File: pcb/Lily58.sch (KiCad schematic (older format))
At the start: 132 parts, among them J2 4PIN, J3 Conn_01x06_Female, J4 Conn_01x06_Female, SW1 SW_PUSH, SW10 SW_PUSH, SW11 SW_PUSH, SW12 SW_PUSH, SW13 SW_PUSH, SW14 SW_PUSH, SW15 SW_PUSH, SW16 SW_PUSH, SW17 SW_PUSH, SW18 SW_PUSH, SW19 SW_PUSH, SW2 SW_PUSH, SW20 SW_PUSH, SW21 SW_PUSH, SW22 SW_PUSH, SW23 SW_PUSH, SW24 SW_PUSH, SW25 SW_PUSH, SW26 SW_PUSH, SW27 SW_PUSH, SW28 SW_PUSH, SW29 SW_PUSH, SW3 SW_PUSH, SW4 SW_PUSH, SW5 SW_PUSH, SW6 SW_PUSH, SW7 SW_PUSH, SW8 SW_PUSH, SW9 SW_PUSH, U1 ProMicro

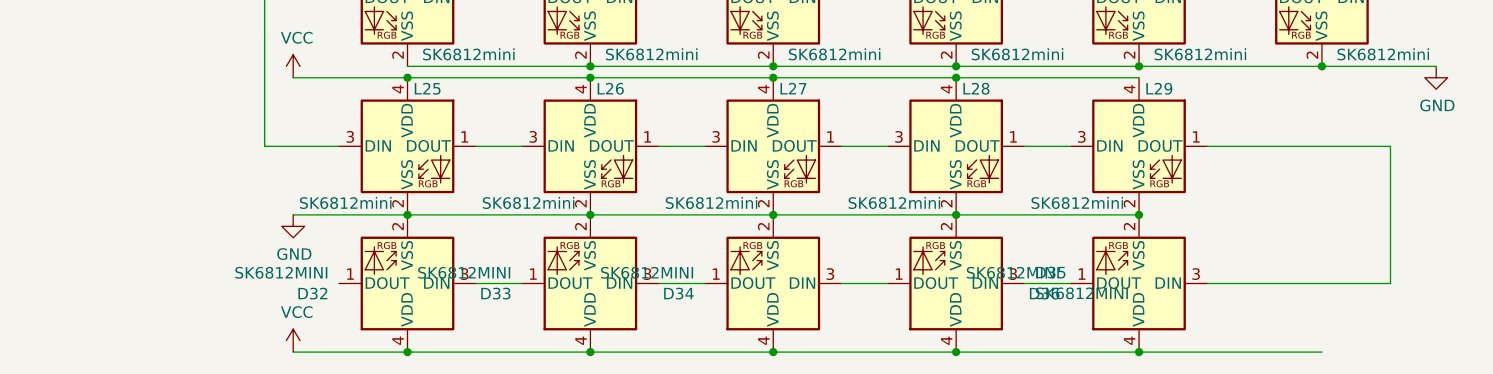
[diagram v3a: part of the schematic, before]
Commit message: refuctor pcb
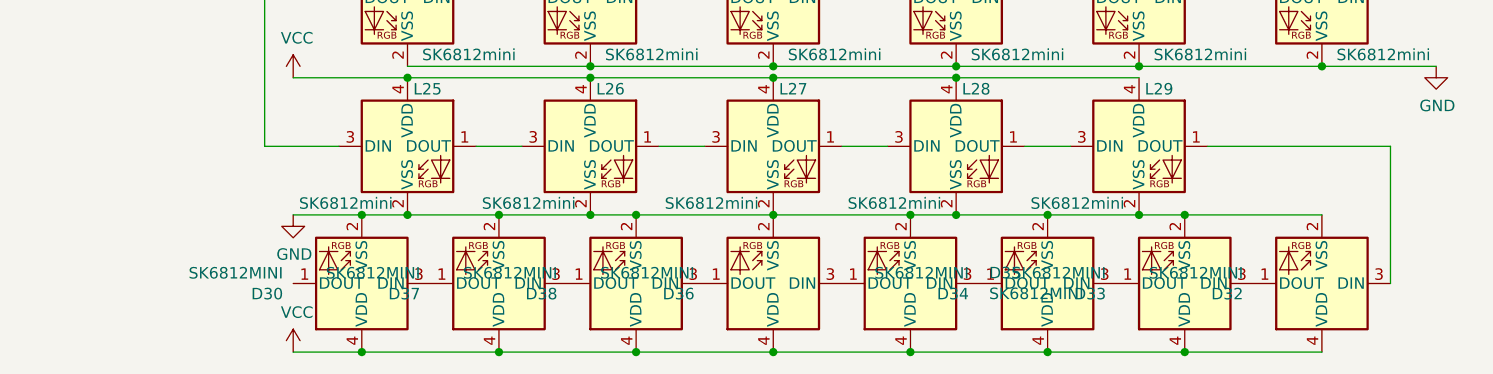
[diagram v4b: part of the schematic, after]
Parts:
- added D30, D37, D38: SK6812MINI, Lily58-footprint:SK6812MINI_underglow_rev, symbol LED:SK6812MINI
- TH3, TH4, TH5, TH6, TH7: footprint Lily58-footprint:HOLE_M2 -> Lily58-footprint:HOLE_M2_TH
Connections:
- net GND: now also D30.2 (VSS), D37.2 (VSS), D38.2 (VSS)
- net VCC: now also D30.4 (VDD), D37.4 (VDD), D38.4 (VDD)
- net at L29.1 (DOUT): now also D32.3 (DIN); no longer D36.3 (DIN)
- net at D35.1 (DOUT): now also D36.3 (DIN); no longer D34.3 (DIN)
- net at D36.1 (DOUT): now also D38.3 (DIN); no longer D35.3 (DIN)
- net at D34.1 (DOUT): now also D35.3 (DIN); no longer D33.3 (DIN)
- net at D33.1 (DOUT): now also D34.3 (DIN); no longer D32.3 (DIN)
- net at D32.1 (DOUT): now also D33.3 (DIN)
- new net: D37.3 (DIN), D38.1 (DOUT)
- new net: D30.3 (DIN), D37.1 (DOUT)
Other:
- moved on the sheet: D32, D33, D34, D35, D36
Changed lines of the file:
@@
 Wire Wire Line
 	6900 9650 7100 9650
-Wire Wire Line
-	7400 9950 8200 9950
 Connection ~ 7400 9950
 Connection ~ 6600 9950
-Wire Wire Line
-	6600 9950 7400 9950
 $Comp
 L LED:SK6812MINI L28
@@
 $EndComp
 Wire Wire Line
-	6600 9950 5800 9950
+	6600 9950 6200 9950
 Wire Wire Line
 	6100 9650 6300 9650
@@
 Wire Wire Line
 	8500 9650 8700 9650
-Wire Wire Line
-	8200 9950 9000 9950
 Connection ~ 8200 9950
 Wire Wire Line
@@
 	2850 8000 2650 8000
 Wire Wire Line
-	5300 9950 5800 9950
+	5300 9950 5600 9950
 Wire Wire Line
 	2350 7000 2800 7000
@@
 	3650 4350 3650 4450
 $Comp
-L Lily58-rescue:HOLE-Lily58-cache TH3
-U 1 1 5B74DA95
-P 8100 6150
-F 0 "TH3" H 8100 6150 60  0000 C CNN
-F 1 "HOLE" H 8100 6050 60  0000 C CNN
-F 2 "Lily58-footprint:HOLE_M2" H 8100 6150 60  0001 C CNN
-F 3 "" H 8100 6150 60  0000 C CNN
-	1    8100 6150
-	1    0    0    -1
-$EndComp
-$Comp
-L Lily58-rescue:HOLE-Lily58-cache TH7
-U 1 1 5B74D98F
-P 9500 6150
-F 0 "TH7" H 9500 6150 60  0000 C CNN
-F 1 "HOLE" H 9500 6050 60  0000 C CNN
-F 2 "Lily58-footprint:HOLE_M2" H 9500 6150 60  0001 C CNN
-F 3 "" H 9500 6150 60  0000 C CNN
-	1    9500 6150
-	1    0    0    -1
-$EndComp
-$Comp
-L Lily58-rescue:HOLE-Lily58-cache TH6
-U 1 1 5B74D88C
-P 9150 6150
-F 0 "TH6" H 9150 6150 60  0000 C CNN
-F 1 "HOLE" H 9150 6050 60  0000 C CNN
-F 2 "Lily58-footprint:HOLE_M2" H 9150 6150 60  0001 C CNN
-F 3 "" H 9150 6150 60  0000 C CNN
-	1    9150 6150
-	1    0    0    -1
-$EndComp
-$Comp
-L Lily58-rescue:HOLE-Lily58-cache TH5
-U 1 1 5B74D78B
-P 8800 6150
-F 0 "TH5" H 8800 6150 60  0000 C CNN
-F 1 "HOLE" H 8800 6050 60  0000 C CNN
-F 2 "Lily58-footprint:HOLE_M2" H 8800 6150 60  0001 C CNN
-F 3 "" H 8800 6150 60  0000 C CNN
-	1    8800 6150
-	1    0    0    -1
-$EndComp
-$Comp
-L Lily58-rescue:HOLE-Lily58-cache TH4
-U 1 1 5B74D1C0
-P 8450 6150
-F 0 "TH4" H 8450 6150 60  0000 C CNN
-F 1 "HOLE" H 8450 6050 60  0000 C CNN
-F 2 "Lily58-footprint:HOLE_M2" H 8450 6150 60  0001 C CNN
-F 3 "" H 8450 6150 60  0000 C CNN
-	1    8450 6150
-	1    0    0    -1
-$EndComp
-$Comp
 L LED:SK6812MINI D35
 U 1 1 6240B7F0
-P 8200 10250
-F 0 "D35" H 7856 10204 50  0000 R CNN
-F 1 "SK6812MINI" H 7856 10295 50  0000 R CNN
-F 2 "Lily58-footprint:SK6812MINI_underglow_rev" H 8250 9950 50  0001 L TNN
-F 3 "https://cdn-shop.adafruit.com/product-files/2686/SK6812MINI_REV.01-1-2.pdf" H 8300 9875 50  0001 L TNN
-	1    8200 10250
+P 8000 10250
+F 0 "D35" H 7656 10204 50  0000 R CNN
+F 1 "SK6812MINI" H 7656 10295 50  0000 R CNN
+F 2 "Lily58-footprint:SK6812MINI_underglow_rev" H 8050 9950 50  0001 L TNN
+F 3 "https://cdn-shop.adafruit.com/product-files/2686/SK6812MINI_REV.01-1-2.pdf" H 8100 9875 50  0001 L TNN
+	1    8000 10250
 	-1   0    0    1
 $EndComp
@@
 L LED:SK6812MINI D34
 U 1 1 62411127
+P 8600 10250
+F 0 "D34" H 8944 10296 50  0000 L CNN
+F 1 "SK6812MINI" H 8944 10205 50  0000 L CNN
+F 2 "Lily58-footprint:SK6812MINI_underglow_rev" H 8650 9950 50  0001 L TNN
+F 3 "https://cdn-shop.adafruit.com/product-files/2686/SK6812MINI_REV.01-1-2.pdf" H 8700 9875 50  0001 L TNN
+	1    8600 10250
+	-1   0    0    1
+$EndComp
+$Comp
+L LED:SK6812MINI D33
+U 1 1 62423173
+P 9200 10250
+F 0 "D33" H 9544 10296 50  0000 L CNN
+F 1 "SK6812MINI" H 9544 10205 50  0000 L CNN
+F 2 "Lily58-footprint:SK6812MINI_underglow_rev" H 9250 9950 50  0001 L TNN
+F 3 "https://cdn-shop.adafruit.com/product-files/2686/SK6812MINI_REV.01-1-2.pdf" H 9300 9875 50  0001 L TNN
+	1    9200 10250
+	-1   0    0    1
+$EndComp
+$Comp
+L LED:SK6812MINI D32
+U 1 1 6245421A
+P 9800 10250
+F 0 "D32" H 10144 10296 50  0000 L CNN
+F 1 "SK6812MINI" H 10144 10205 50  0000 L CNN
+F 2 "Lily58-footprint:SK6812MINI_underglow_rev" H 9850 9950 50  0001 L TNN
+F 3 "https://cdn-shop.adafruit.com/product-files/2686/SK6812MINI_REV.01-1-2.pdf" H 9900 9875 50  0001 L TNN
+	1    9800 10250
+	-1   0    0    1
+$EndComp
+$Comp
+L LED:SK6812MINI D36
+U 1 1 624C4CC2
 P 7400 10250
-F 0 "D34" H 7744 10296 50  0000 L CNN
+F 0 "D36" H 7744 10296 50  0000 L CNN
 F 1 "SK6812MINI" H 7744 10205 50  0000 L CNN
 F 2 "Lily58-footprint:SK6812MINI_underglow_rev" H 7450 9950 50  0001 L TNN
@@
 	-1   0    0    1
 $EndComp
-$Comp
-L LED:SK6812MINI D33
-U 1 1 62423173
-P 6600 10250
-F 0 "D33" H 6944 10296 50  0000 L CNN
-F 1 "SK6812MINI" H 6944 10205 50  0000 L CNN
-F 2 "Lily58-footprint:SK6812MINI_underglow_rev" H 6650 9950 50  0001 L TNN
-F 3 "https://cdn-shop.adafruit.com/product-files/2686/SK6812MINI_REV.01-1-2.pdf" H 6700 9875 50  0001 L TNN
-	1    6600 10250
-	-1   0    0    1
-$EndComp
-Connection ~ 9000 9950
-$Comp
-L LED:SK6812MINI D32
-U 1 1 6245421A
-P 5800 10250
-F 0 "D32" H 6144 10296 50  0000 L CNN
-F 1 "SK6812MINI" H 6144 10205 50  0000 L CNN
-F 2 "Lily58-footprint:SK6812MINI_underglow_rev" H 5850 9950 50  0001 L TNN
-F 3 "https://cdn-shop.adafruit.com/product-files/2686/SK6812MINI_REV.01-1-2.pdf" H 5900 9875 50  0001 L TNN
-	1    5800 10250
-	-1   0    0    1
-$EndComp
-Wire Wire Line
-	6100 10250 6300 10250
-Wire Wire Line
-	7100 10250 6900 10250
-Wire Wire Line
-	7700 10250 7900 10250
-$Comp
-L LED:SK6812MINI D36
-U 1 1 624C4CC2
-P 9000 10250
-F 0 "D36" H 9344 10296 50  0000 L CNN
-F 1 "SK6812MINI" H 9344 10205 50  0000 L CNN
-F 2 "Lily58-footprint:SK6812MINI_underglow_rev" H 9050 9950 50  0001 L TNN
-F 3 "https://cdn-shop.adafruit.com/product-files/2686/SK6812MINI_REV.01-1-2.pdf" H 9100 9875 50  0001 L TNN
-	1    9000 10250
-	-1   0    0    1
-$EndComp
-Wire Wire Line
-	8500 10250 8700 10250
 Wire Wire Line
 	9300 9650 10100 9650
 Wire Wire Line
 	10100 9650 10100 10250
-Wire Wire Line
-	9800 10550 9000 10550
-Connection ~ 6600 10550
-Connection ~ 7400 10550
-Wire Wire Line
-	7400 10550 6600 10550
-Connection ~ 8200 10550
-Wire Wire Line
-	8200 10550 7400 10550
-Connection ~ 9000 10550
-Wire Wire Line
-	9000 10550 8200 10550
 $Comp
 L power:VCC #PWR0115
@@
 	1    0    0    -1
 $EndComp
-Wire Wire Line
-	5300 10550 5800 10550
-Connection ~ 5800 10550
-Wire Wire Line
-	5800 10550 6600 10550
-Wire Wire Line
-	9300 10250 10100 10250
+$Comp
+L Lily58-rescue:HOLE-Lily58-cache TH4
+U 1 1 5B74D1C0
+P 8450 6150
+F 0 "TH4" H 8450 6150 60  0000 C CNN
+F 1 "HOLE" H 8450 6050 60  0000 C CNN
+F 2 "Lily58-footprint:HOLE_M2_TH" H 8450 6150 60  0001 C CNN
+F 3 "" H 8450 6150 60  0000 C CNN
+	1    8450 6150
+	1    0    0    -1
+$EndComp
+$Comp
+L Lily58-rescue:HOLE-Lily58-cache TH5
+U 1 1 5B74D78B
+P 8800 6150
+F 0 "TH5" H 8800 6150 60  0000 C CNN
+F 1 "HOLE" H 8800 6050 60  0000 C CNN
+F 2 "Lily58-footprint:HOLE_M2_TH" H 8800 6150 60  0001 C CNN
+F 3 "" H 8800 6150 60  0000 C CNN
+	1    8800 6150
+	1    0    0    -1
+$EndComp
+$Comp
+L Lily58-rescue:HOLE-Lily58-cache TH6
+U 1 1 5B74D88C
+P 9150 6150
+F 0 "TH6" H 9150 6150 60  0000 C CNN
+F 1 "HOLE" H 9150 6050 60  0000 C CNN
+F 2 "Lily58-footprint:HOLE_M2_TH" H 9150 6150 60  0001 C CNN
+F 3 "" H 9150 6150 60  0000 C CNN
+	1    9150 6150
+	1    0    0    -1
+$EndComp
+$Comp
+L Lily58-rescue:HOLE-Lily58-cache TH7
+U 1 1 5B74D98F
+P 9500 6150
+F 0 "TH7" H 9500 6150 60  0000 C CNN
+F 1 "HOLE" H 9500 6050 60  0000 C CNN
+F 2 "Lily58-footprint:HOLE_M2_TH" H 9500 6150 60  0001 C CNN
+F 3 "" H 9500 6150 60  0000 C CNN
+	1    9500 6150
+	1    0    0    -1
+$EndComp
+$Comp
+L Lily58-rescue:HOLE-Lily58-cache TH3
+U 1 1 5B74DA95
+P 8100 6150
+F 0 "TH3" H 8100 6150 60  0000 C CNN
+F 1 "HOLE" H 8100 6050 60  0000 C CNN
+F 2 "Lily58-footprint:HOLE_M2_TH" H 8100 6150 60  0001 C CNN
+F 3 "" H 8100 6150 60  0000 C CNN
+	1    8100 6150
+	1    0    0    -1
+$EndComp
+Connection ~ 7400 10550
+Connection ~ 8000 9950
+Wire Wire Line
+	8000 9950 8200 9950
+Connection ~ 8000 10550
+Connection ~ 8600 9950
+Wire Wire Line
+	8600 9950 9000 9950
+Connection ~ 8600 10550
+Wire Wire Line
+	7400 9950 8000 9950
+Wire Wire Line
+	6600 9950 6800 9950
+Wire Wire Line
+	8200 9950 8600 9950
+Wire Wire Line
+	5300 10550 5600 10550
+Wire Wire Line
+	7400 10550 8000 10550
+Wire Wire Line
+	8000 10550 8600 10550
+Wire Wire Line
+	8600 10550 9200 10550
+Connection ~ 9200 10550
+Wire Wire Line
+	9200 10550 9800 10550
+Wire Wire Line
+	9800 9950 9200 9950
+Connection ~ 9000 9950
+Connection ~ 9200 9950
+Wire Wire Line
+	9200 9950 9000 9950
+$Comp
+L LED:SK6812MINI D38
+U 1 1 61D96A0F
+P 6800 10250
+F 0 "D38" H 7144 10296 50  0000 L CNN
+F 1 "SK6812MINI" H 7144 10205 50  0000 L CNN
+F 2 "Lily58-footprint:SK6812MINI_underglow_rev" H 6850 9950 50  0001 L TNN
+F 3 "https://cdn-shop.adafruit.com/product-files/2686/SK6812MINI_REV.01-1-2.pdf" H 6900 9875 50  0001 L TNN
+	1    6800 10250
+	-1   0    0    1
+$EndComp
+Connection ~ 6800 9950
+Wire Wire Line
+	6800 9950 7400 9950
+Connection ~ 6800 10550
+Wire Wire Line
+	6800 10550 7400 10550
+$Comp
+L LED:SK6812MINI D37
+U 1 1 61D98064
+P 6200 10250
+F 0 "D37" H 6544 10296 50  0000 L CNN
+F 1 "SK6812MINI" H 6544 10205 50  0000 L CNN
+F 2 "Lily58-footprint:SK6812MINI_underglow_rev" H 6250 9950 50  0001 L TNN
+F 3 "https://cdn-shop.adafruit.com/product-files/2686/SK6812MINI_REV.01-1-2.pdf" H 6300 9875 50  0001 L TNN
+	1    6200 10250
+	-1   0    0    1
+$EndComp
+Connection ~ 6200 9950
+Wire Wire Line
+	6200 9950 5800 9950
+Connection ~ 6200 10550
+Wire Wire Line
+	6200 10550 6800 10550
+$Comp
+L LED:SK6812MINI D30
+U 1 1 61D997AB
+P 5600 10250
+F 0 "D30" H 5944 10296 50  0000 L CNN
+F 1 "SK6812MINI" H 5944 10205 50  0000 L CNN
+F 2 "Lily58-footprint:SK6812MINI_underglow_rev" H 5650 9950 50  0001 L TNN
+F 3 "https://cdn-shop.adafruit.com/product-files/2686/SK6812MINI_REV.01-1-2.pdf" H 5700 9875 50  0001 L TNN
+	1    5600 10250
+	-1   0    0    1
+$EndComp
+Connection ~ 5600 9950
+Wire Wire Line
+	5600 9950 5800 9950
+Connection ~ 5600 10550
+Wire Wire Line
+	5600 10550 6200 10550
 $EndSCHEMATC

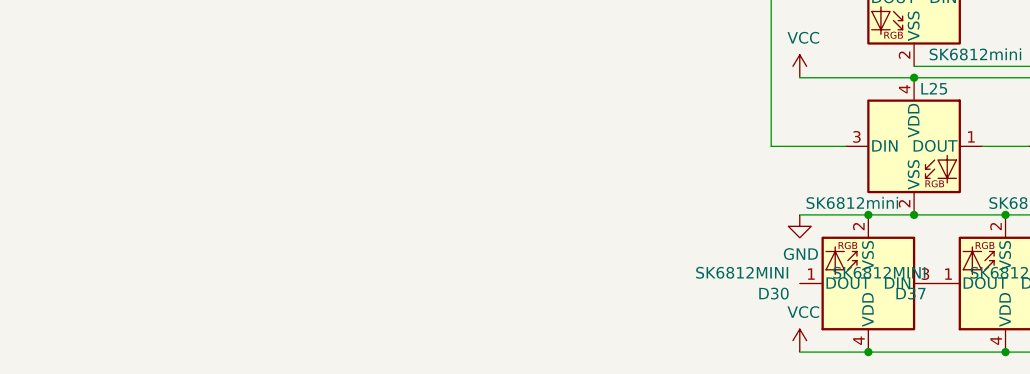
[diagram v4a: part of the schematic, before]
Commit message: add underglow
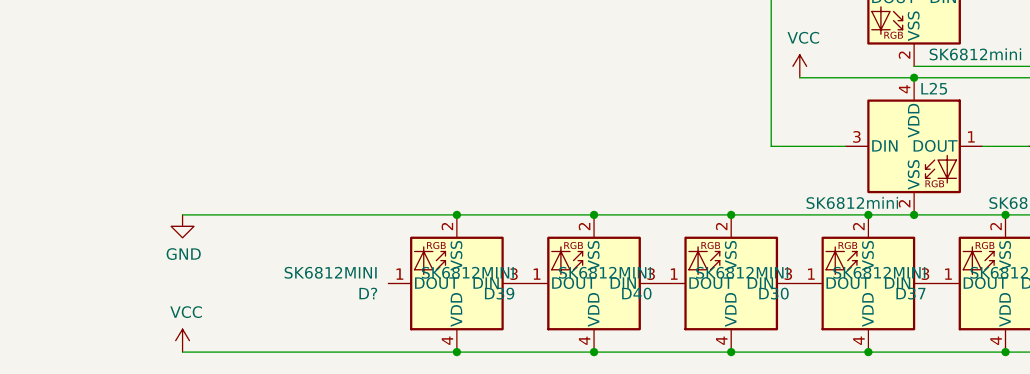
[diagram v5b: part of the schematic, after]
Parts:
- added D39, D40, D?: SK6812MINI, Lily58-footprint:SK6812MINI_underglow_rev, symbol LED:SK6812MINI
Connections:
- net GND: now also D39.2 (VSS), D40.2 (VSS), D?.2 (VSS)
- net VCC: now also D39.4 (VDD), D40.4 (VDD), D?.4 (VDD)
- net at D30.1 (DOUT): now also D40.3 (DIN)
- new net: D39.3 (DIN), D40.1 (DOUT)
- new net: D39.1 (DOUT), D?.3 (DIN)
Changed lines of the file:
@@
 L power:GND #PWR0105
 U 1 1 5D44C2B9
-P 5300 9950
-F 0 "#PWR0105" H 5300 9700 50  0001 C CNN
-F 1 "GND" H 5305 9777 50  0000 C CNN
-F 2 "" H 5300 9950 50  0001 C CNN
-F 3 "" H 5300 9950 50  0001 C CNN
-	1    5300 9950
+P 2600 9950
+F 0 "#PWR0105" H 2600 9700 50  0001 C CNN
+F 1 "GND" H 2605 9777 50  0000 C CNN
+F 2 "" H 2600 9950 50  0001 C CNN
+F 3 "" H 2600 9950 50  0001 C CNN
+	1    2600 9950
 	1    0    0    -1
 $EndComp
@@
 Wire Wire Line
 	2850 8000 2650 8000
-Wire Wire Line
-	5300 9950 5600 9950
 Wire Wire Line
 	2350 7000 2800 7000
@@
 L power:VCC #PWR0115
 U 1 1 62526079
-P 5300 10550
-F 0 "#PWR0115" H 5300 10400 50  0001 C CNN
-F 1 "VCC" H 5317 10723 50  0000 C CNN
-F 2 "" H 5300 10550 50  0001 C CNN
-F 3 "" H 5300 10550 50  0001 C CNN
-	1    5300 10550
+P 2600 10550
+F 0 "#PWR0115" H 2600 10400 50  0001 C CNN
+F 1 "VCC" H 2617 10723 50  0000 C CNN
+F 2 "" H 2600 10550 50  0001 C CNN
+F 3 "" H 2600 10550 50  0001 C CNN
+	1    2600 10550
 	1    0    0    -1
 $EndComp
@@
 Wire Wire Line
 	8200 9950 8600 9950
-Wire Wire Line
-	5300 10550 5600 10550
 Wire Wire Line
 	7400 10550 8000 10550
@@
 Wire Wire Line
 	5600 10550 6200 10550
+$Comp
+L LED:SK6812MINI D40
+U 1 1 61DD4E2C
+P 5000 10250
+F 0 "D40" H 5344 10296 50  0000 L CNN
+F 1 "SK6812MINI" H 5344 10205 50  0000 L CNN
+F 2 "Lily58-footprint:SK6812MINI_underglow_rev" H 5050 9950 50  0001 L TNN
+F 3 "https://cdn-shop.adafruit.com/product-files/2686/SK6812MINI_REV.01-1-2.pdf" H 5100 9875 50  0001 L TNN
+	1    5000 10250
+	-1   0    0    1
+$EndComp
+$Comp
+L LED:SK6812MINI D39
+U 1 1 61DD4E32
+P 4400 10250
+F 0 "D39" H 4744 10296 50  0000 L CNN
+F 1 "SK6812MINI" H 4744 10205 50  0000 L CNN
+F 2 "Lily58-footprint:SK6812MINI_underglow_rev" H 4450 9950 50  0001 L TNN
+F 3 "https://cdn-shop.adafruit.com/product-files/2686/SK6812MINI_REV.01-1-2.pdf" H 4500 9875 50  0001 L TNN
+	1    4400 10250
+	-1   0    0    1
+$EndComp
+Wire Wire Line
+	4400 9950 5000 9950
+Connection ~ 5000 9950
+Wire Wire Line
+	5000 9950 5600 9950
+Wire Wire Line
+	4400 10550 5000 10550
+Connection ~ 5000 10550
+Wire Wire Line
+	5000 10550 5600 10550
+$Comp
+L LED:SK6812MINI D?
+U 1 1 61E99363
+P 3800 10250
+F 0 "D?" H 4144 10296 50  0000 L CNN
+F 1 "SK6812MINI" H 4144 10205 50  0000 L CNN
+F 2 "Lily58-footprint:SK6812MINI_underglow_rev" H 3850 9950 50  0001 L TNN
+F 3 "https://cdn-shop.adafruit.com/product-files/2686/SK6812MINI_REV.01-1-2.pdf" H 3900 9875 50  0001 L TNN
+	1    3800 10250
+	-1   0    0    1
+$EndComp
+Wire Wire Line
+	2600 9950 3800 9950
+Connection ~ 4400 9950
+Connection ~ 3800 9950
+Wire Wire Line
+	3800 9950 4400 9950
+Wire Wire Line
+	2600 10550 3800 10550
+Connection ~ 4400 10550
+Connection ~ 3800 10550
+Wire Wire Line
+	3800 10550 4400 10550
 $EndSCHEMATC
